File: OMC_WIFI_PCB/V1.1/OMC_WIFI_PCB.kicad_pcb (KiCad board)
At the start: 2 copper layers, 103.2 x 83.1 mm, 18 parts, among them J1 ESP32_Left, J10 Control_ACS712, J11 Control_ZMPT101B, J2 ESP32_Right, J3 Power_In, J4 Switch, J5 Pins_FT232R, J6 Line_Relay, J7 Control_Relay, J8 Line_ACS712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

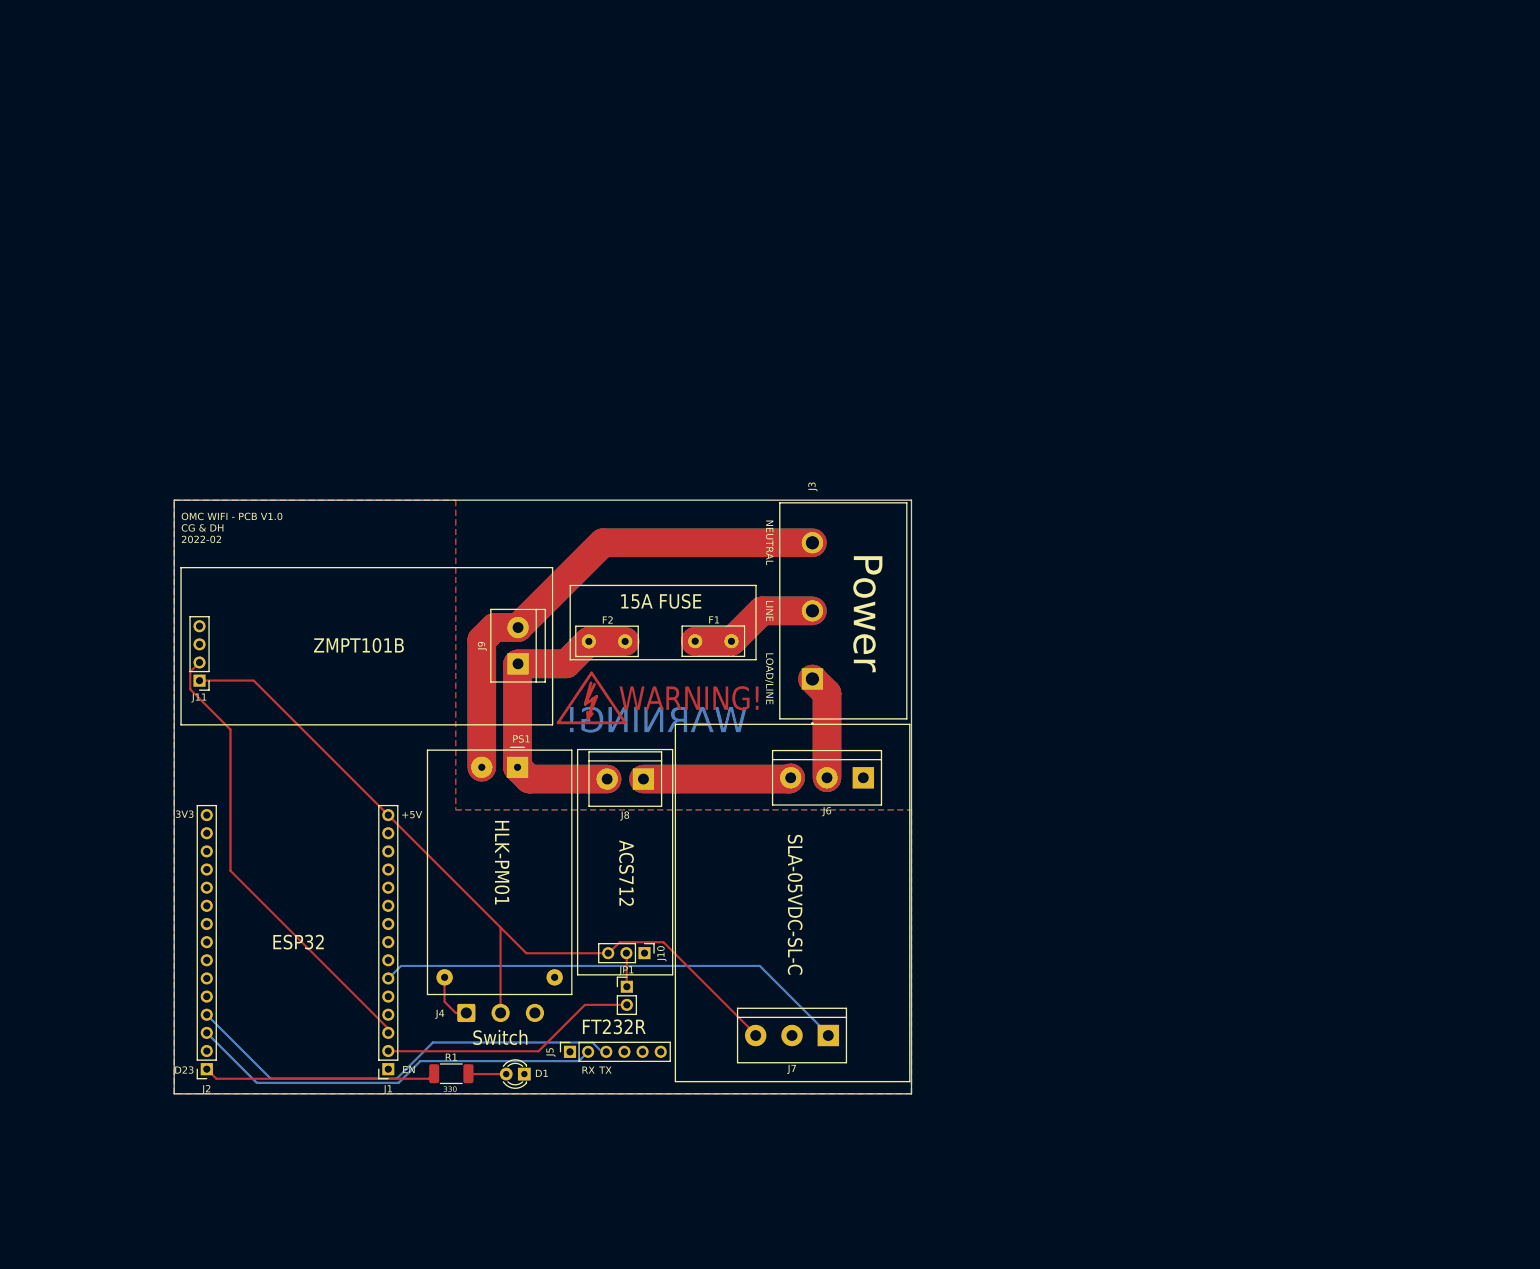
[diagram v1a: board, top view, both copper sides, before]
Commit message: Actualización PCB v1.1
+ Alimentación (Input/Output)
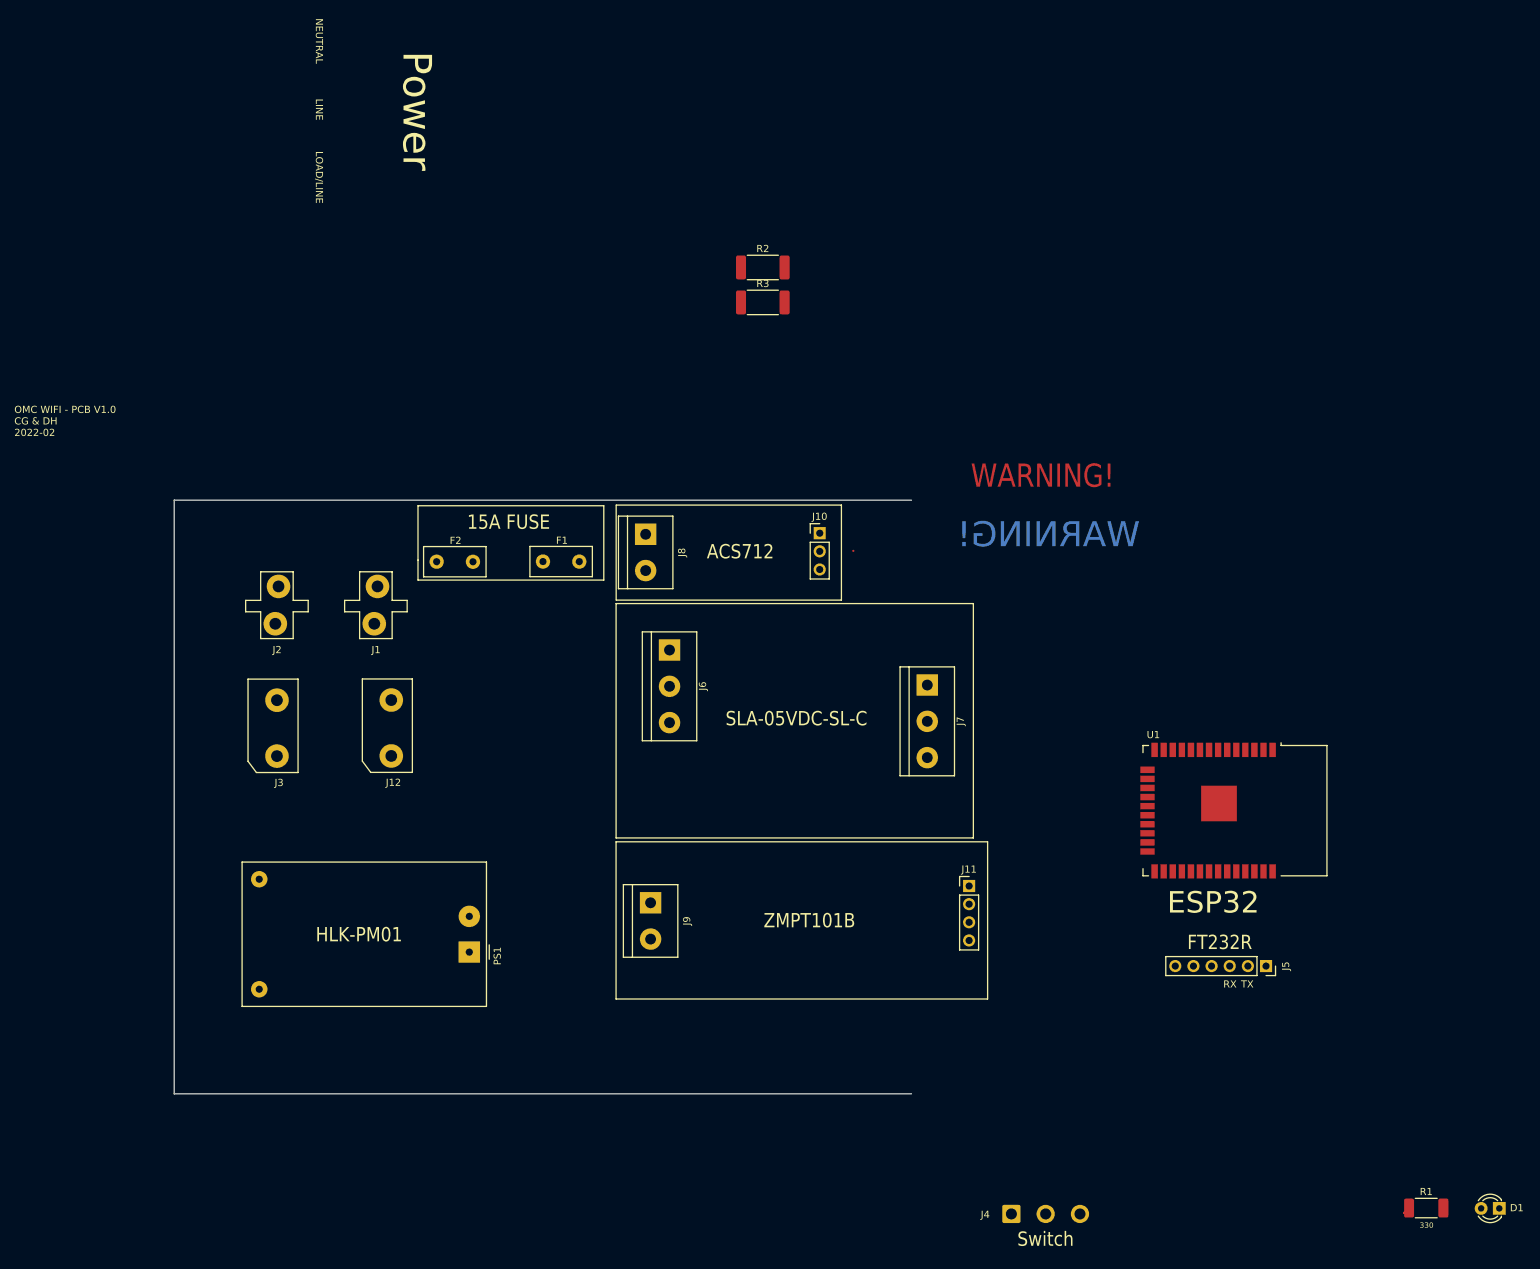
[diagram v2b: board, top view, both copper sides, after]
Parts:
- removed JP1: Jumper, Connector_PinHeader_2.54mm:PinHeader_1x02_P2.54mm_Vertical
- removed REF**: Symbol_HighVoltage_Type2_CopperTop_VerySmall, Symbol:Symbol_HighVoltage_Type2_CopperTop_VerySmall
- added J12: Nuetral Output, omc-plugs:OMC-Female-Plug, F.Cu at (606.3, -950.0)
- added R2: 1K, Resistor_SMD:R_2512_6332Metric_Pad1.40x3.35mm_HandSolder, F.Cu at (659.0, -1014.5)
- added R3: 2K, Resistor_SMD:R_2512_6332Metric_Pad1.40x3.35mm_HandSolder, F.Cu at (659.0, -1009.6)
- added U1: ESP32-WROOM-32, RF_Module:ESP32-WROOM-32, F.Cu at (722.0, -938.5)
- J1: value ESP32_Left -> Line Input; footprint Connector_PinSocket_2.54mm:PinSocket_1x15_P2.54mm_Vertical -> omc-plugs:OMC-Male-Plug
- J2: value ESP32_Right -> Nuetral Input; footprint Connector_PinSocket_2.54mm:PinSocket_1x15_P2.54mm_Vertical -> omc-plugs:OMC-Male-Plug
- J3: value Power_In -> Line Output; footprint 6PCV-03-006:TE_5-1437652-4 -> omc-plugs:OMC-Female-Plug
- moved D1 137.7 mm to (762.0, -882.8)
- moved R1 137.7 mm to (751.8, -882.9)
- moved J11 111.5 mm to (687.8, -927.9), turned to 0 degrees
- moved J5 98.1 mm to (729.4, -916.7), turned to 270 degrees
- moved J4 81.3 mm to (693.7, -882.0)
- moved J3 75.9 mm to (590.3, -950.0), turned to 0 degrees
- moved J2 65.4 mm to (591.0, -967.0), turned to 0 degrees
- moved J1 64.7 mm to (604.8, -967.0), turned to 0 degrees
- moved J10 63.7 mm to (666.9, -977.3), turned to 0 degrees
- moved J7 51.0 mm to (682.0, -956.1), turned to 270 degrees
- moved J9 38.2 mm to (643.2, -925.6), turned to 270 degrees
- moved J8 34.3 mm to (642.6, -977.2), turned to 270 degrees
- moved J6 32.5 mm to (645.9, -961.0), turned to 270 degrees
- moved PS1 26.7 mm to (617.9, -918.7), turned to 180 degrees
- moved F2 24.0 mm to (613.3, -973.3)
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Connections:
- J1 pad 1: EN -> Net-(F1-Pad1)
- J1 pad 2: VP_ACS -> (no net)
- J10 pad 2: Net-(J10-Pad2) -> VP_ACS
- J2 pad 1: D23_LED -> NEUTRAL
- J2 pad 2: D22 -> (no net)
- J3 pad 1: COM -> Net-(J3-Pad1)
- PS1 pad 1: LINE -> Neutral
- PS1 pad 2: NEUTRAL -> Line
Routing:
- net NEUTRAL: track 139.4 -> 0.00 mm
- net +5V: track 111.7 -> 0.00 mm
- net LINE: track 88.1 -> 0.00 mm
- net D32_RELAY: track 66.4 -> 0.00 mm
- net VN_ZMPT: track 63.9 -> 0.00 mm
- net RX0: track 62.2 -> 0.62 mm
- net TX0: track 58.1 -> 0.00 mm
- net NO: track 41.4 -> 0.00 mm
- net Net-(F1-Pad1): track 36.4 -> 0.00 mm
- net VP_ACS: track 36.1 -> 0.00 mm
- net D23_LED: track 33.6 -> 1.97 mm
- net COM: track 29.3 -> 0.00 mm
- net Net-(J4-Pad1): track 7.10 -> 0.00 mm
- net Net-(D1-Pad2): track 5.38 -> 0.14 mm
- net Net-(J10-Pad2): track 4.69 -> 0.01 mm
- removed copper zone on B.Cu, net GND
- removed copper zone on F.Cu, net GND
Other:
- board text removed: "+5V"
- board text removed: "3V3"
- board text removed: "D23"
- board text removed: "EN"

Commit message: Actualización PCB
> Divisores de tensión
> Nuevos Gerbers
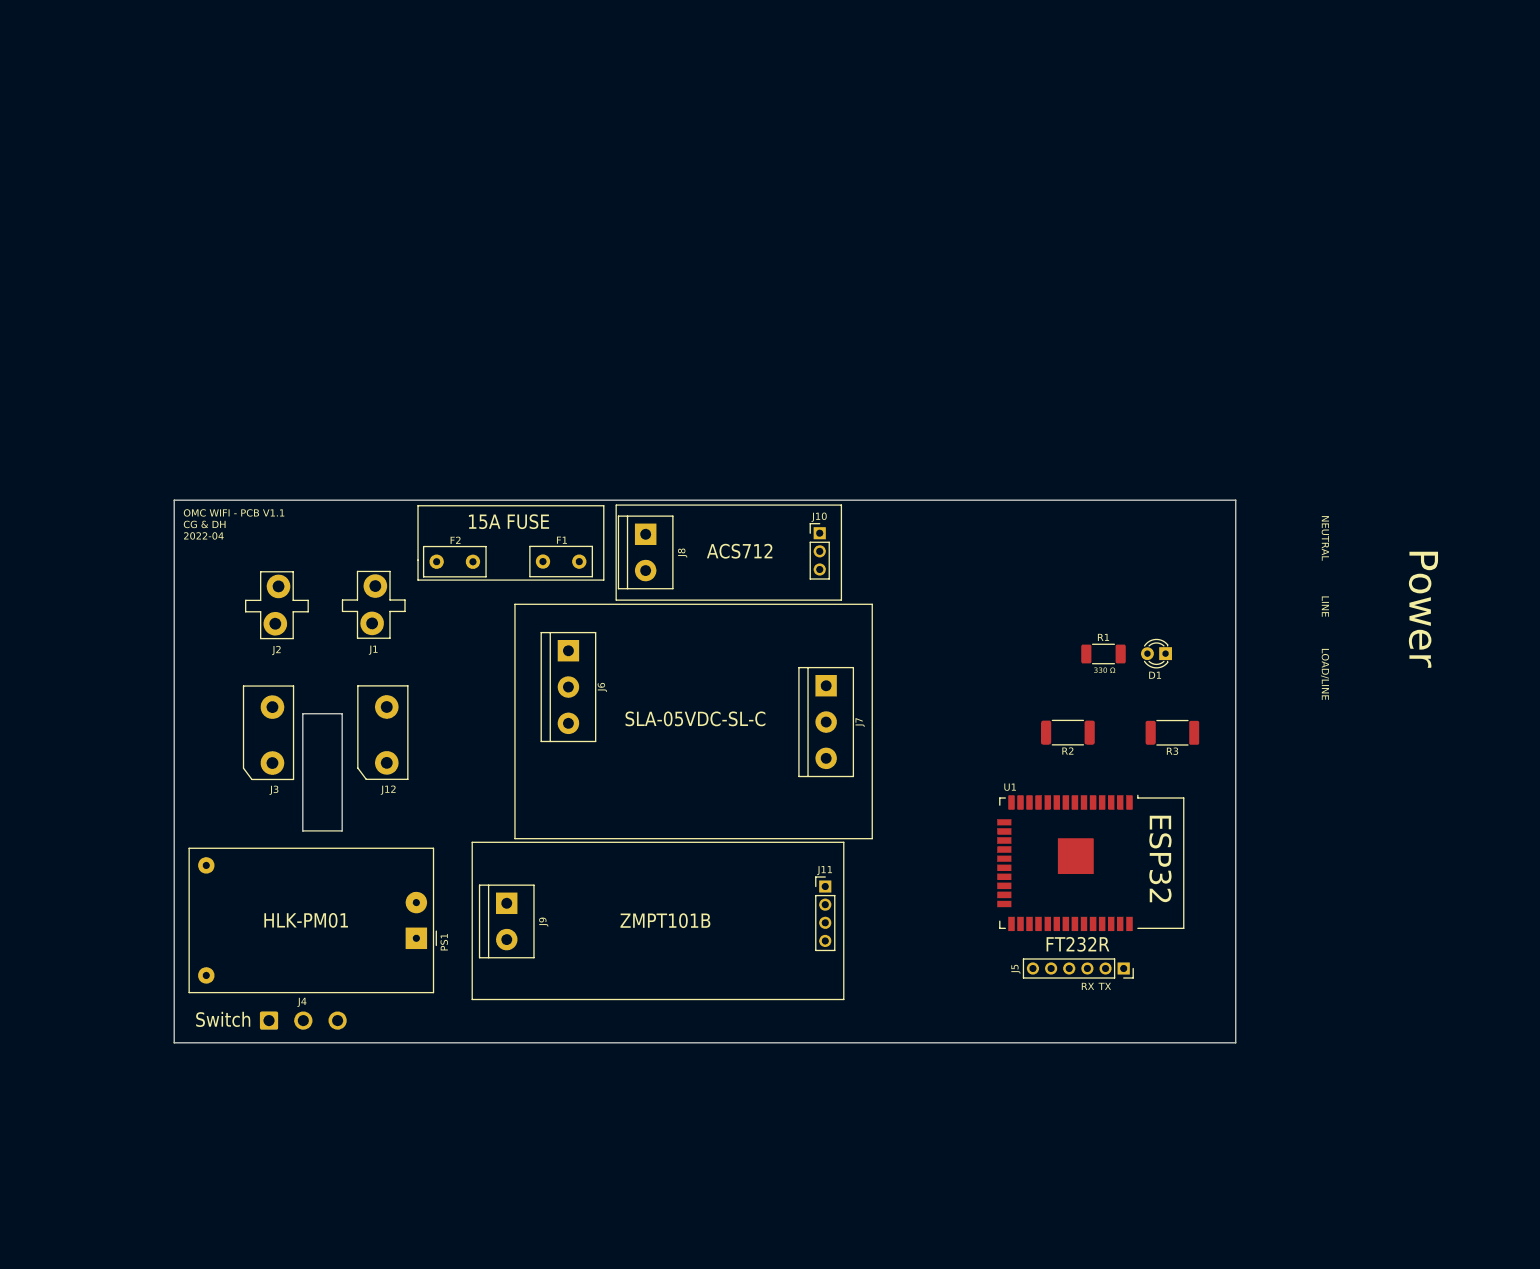
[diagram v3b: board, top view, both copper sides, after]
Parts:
- moved J4 107.4 mm to (589.9, -909.1)
- moved D1 90.6 mm to (715.3, -960.5)
- moved R1 89.7 mm to (706.6, -960.4)
- moved R3 83.1 mm to (716.3, -949.4), turned to 180 degrees
- moved R2 77.8 mm to (701.6, -949.4), turned to 180 degrees
- moved U1 21.3 mm to (702.0, -931.1)
- moved J11 20.1 mm to (667.7, -927.9)
- moved J9 20.1 mm to (623.1, -925.5)
- moved J5 19.9 mm to (709.5, -916.4)
- moved J6 14.2 mm to (631.8, -960.9)
- moved J7 14.2 mm to (667.8, -956.0)
- moved PS1 7.66 mm to (610.5, -920.6)
- moved J12 1.16 mm to (605.7, -949.0)
- moved J3 1.16 mm to (589.7, -949.0)
- moved J1 0.30 mm to (604.5, -967.0)
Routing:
- net D23_LED: track 1.97 -> 0.00 mm
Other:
- board size 103.2 x 83.1 mm -> 148.6 x 75.9 mm
- board text added: "330 Ω"
- board text added: "OMC WIFI - PCB V1.1 CG & DH 2022-04"
- board text removed: "330"
- board text removed: "OMC WIFI - PCB V1.0 CG & DH 2022-02"
- board text removed: "WARNING!"
